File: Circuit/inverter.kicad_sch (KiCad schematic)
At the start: 2 parts, among them Q6 NPN

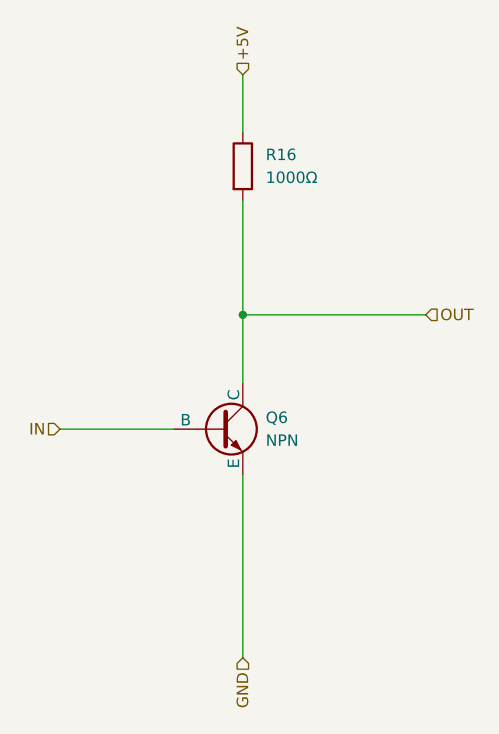
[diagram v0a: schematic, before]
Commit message: Added support for 2 power supplies (5V and 0-30V) and used mosfets
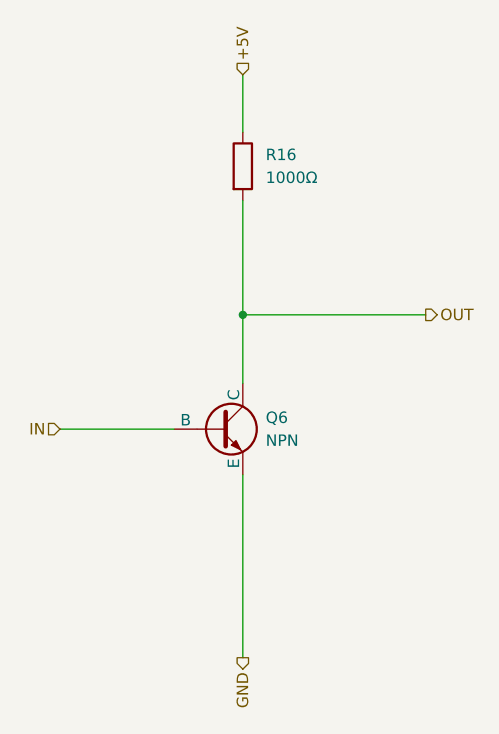
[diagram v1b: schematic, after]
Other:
- title: (none) -> ASR 2024 - Digital Signal Inverter
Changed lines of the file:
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@@
 	(paper "A4")
 	(title_block
-		(date "2024-09-25")
-		(rev "v0.0.5")
+		(title "ASR 2024 - Digital Signal Inverter")
+		(date "2024-09-30")
+		(rev "v0.1.0")
 		(company "Alexandre Haddad-Delaveau & Bryan Liu")
-		(comment 1 "Pinout of transistors and hall chips are subject to change.")
+		(comment 1 "Pinouts are subject to change.")
 		(comment 2 "Resistor values are subject to change.")
 		(comment 3 "Warning:")
@@
 	)
 	(hierarchical_label "OUT"
-		(shape input)
+		(shape output)
 		(at 116.84 88.9 0)
 		(fields_autoplaced yes)
@@
 	)
 	(hierarchical_label "GND"
-		(shape input)
+		(shape output)
 		(at 96.52 127 270)
 		(fields_autoplaced yes)
@@
 					(unit 1)
 				)
+				(path "/75cb3666-e798-47d5-a64e-682dd769d21a/34174c80-1df9-4754-82c6-539d1074b657"
+					(reference "R?")
+					(unit 1)
+				)
 				(path "/75cb3666-e798-47d5-a64e-682dd769d21a/f304899a-546b-4342-945f-896799fe9f4e"
 					(reference "R17")
@@
 					(unit 1)
 				)
+				(path "/75cb3666-e798-47d5-a64e-682dd769d21a/34174c80-1df9-4754-82c6-539d1074b657"
+					(reference "Q?")
+					(unit 1)
+				)
